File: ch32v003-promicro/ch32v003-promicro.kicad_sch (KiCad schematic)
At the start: 20 parts, among them J1 USB2.0_C_v3, J2 ProMicro-LeftPin, J3 ProMicro-RightPin, SW1 SW_Push, U1 CH32V003F4P6, U2 AMS1117-3.3, Y1 24M

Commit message: ch32v003promicro/1.0.0
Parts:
- added JP1: SolderJumper_2_Open, Jumper:SolderJumper-2_P1.3mm_Open_RoundedPad1.0x1.5mm, symbol Jumper:SolderJumper_2_Open
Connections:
- net +5V: now also JP1.1 (A)
- net +3V3 renamed VCC
- net VCC: now also JP1.2 (B)

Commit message: ch32v003promicro/1.1.0
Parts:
- removed C4, C5: 22p, $74th:Capacitor_0805_2012, symbol Device:C
- removed Y1: 24M, $74th:Crystal_SMD_3225-4Pin_3.2x2.5mm_HandSoldering, symbol Device:Crystal_GND24
- added C6: 1u, $74th:Capacitor_0805_2012, symbol Device:C
- added J2: SWD-MCU_Side-10Pin, $74th:SWD_2x05_P1.27mm, symbol $74th:SWD-MCU_Side-10Pin
- added R1: 10k, $74th:Register_0805_2012, symbol Device:R
- added R2: 54k, $74th:Register_0805_2012, symbol Device:R
- added R5: 1.5k(NC), $74th:Register_0805_2012, symbol Device:R
- added R6, R7: 27.4(NC), $74th:Register_0805_2012, symbol Device:R
- added U3: CH217K, Package_TO_SOT_SMD:SOT-23-6, symbol $74th:CH217K-USB_Power_Limit_Switch
- C2: renamed from C7; value 2.2u -> 10u
- D1: value LED -> Blue
- R10: renamed from R4; value 200 -> 10k
- renumbered C6 to C1, C1 to C3, C2 to C4, C3 to C5, J2 to J3, J3 to J4, R2 to R4, R5 to R8, R1 to R9, U2 to U1, U1 to U2
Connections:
- net +5V: now also U3.1 (VOUT); no longer J1.1 (VBUS)
- net 0/UART_RX: now also J2.7 (RXD)
- net 10/A10: now also U2.14 (PC4/ADC2); no longer U2.19 (PD2/ADC3)
- net 18/A0: now also U2.19 (PD2/ADC3); no longer U2.6 (PA2/ADC0/OSC_OUT)
- net 19/A1: now also U2.20 (PD3/UART_CTS/ADC4), R6.2; no longer U2.5 (PA1/ADC1/OSC_IN)
- net 1/UART_TX: now also J2.8 (TXD)
- net 21/A3: now also J2.2 (SWDIO)
- net 4/A6: now also U2.1 (PD4/UART_CK/ADC7), R7.2; no longer U2.20 (PD3/UART_CTS/ADC4)
- net 5: now also U2.5 (PA1/ADC1/OSC_IN); no longer U2.13 (PC3)
- net 6/A7: now also U2.6 (PA2/ADC0/OSC_OUT); no longer U2.1 (PD4/UART_CK/ADC7)
- net 7: now also U2.8 (PD0); no longer U2.10 (PC0)
- net 8/A8: now also U2.10 (PC0); no longer U2.8 (PD0)
- net 9/A9: now also U2.13 (PC3); no longer U2.14 (PC4/ADC2)
- net GND: now also C6.2, J2.3 (GND), J2.5 (GND), J2.9 (GND), R1.2, R2.2, U3.2 (GND)
- net RST: now also J2.10 (~{RESET})
- net VCC: now also C6.1, J2.1 (VCC), R5.1
- net USB_D-: now reaches J1.2 (D-)
- net USB_D-: now also R5.2, R6.1
- net USB_D+: now reaches J1.3 (D+)
- net USB_D+: now also R7.1
- net 16/SPI_MOSI renamed 16/SPL_MOSI
- new net: R1.1, U3.4 (EN#)
- new net: J1.1 (VBUS), U3.6 (VIN)
- new net: R2.1, U3.5 (ISET)
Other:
- note added: "CH32V003"
- note added: "ProMicro Pin"
- note added: "SWD 10pin with UART"
- note added: "USB"
- note added: "USB Data"
- note added: "VCC 5V Jumper"
- note added: "VCC Select"
- moved on the sheet: C1, C2, C3, C4, C5, D1, J1, JP1, R10, R3, R4, R8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

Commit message: ch32v003promicro/1.2.0
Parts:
- removed R1: 10k, $74th:Register_0805_2012, symbol Device:R
- removed R2: 54k, $74th:Register_0805_2012, symbol Device:R
- removed U3: CH217K, Package_TO_SOT_SMD:SOT-23-6, symbol $74th:CH217K-USB_Power_Limit_Switch
- added U3: CH213K, 74th:Package_SOT-23, symbol 74th_Passive:CH213K_Ideal-Diode-for-USB-Power
- C1, C2, C3, C4, C5, C6: footprint $74th:Capacitor_0805_2012 -> 74th:Capacitor_0805_2012
- D1: footprint $74th:LED_0805_2012Metric_Pad1.15x1.40mm_HandSolder -> 74th:LED_0805_2012
- J1: footprint $74th:USB-C-12-Pin-SMD -> 74th:Connector_USB-C-Receptacle_SMT_12-Pin_Simple
- J2: footprint $74th:SWD_2x05_P1.27mm -> 74th:Connector_HalfPinHeader_SWD
- J3: footprint $74th:ProMicro_LIKE_LEFT -> 74th:PinOut_ProMicro-LIKE_LEFT
- J4: footprint $74th:ProMicro_LIKE_RIGHT -> 74th:PinOut_ProMicro-LIKE_RIGHT
- R10, R3, R4, R5, R6, R7, R8, R9: footprint $74th:Register_0805_2012 -> 74th:Register_0805_2012
- SW1: footprint $74th:SKRPABE010 -> 74th:PushButton_SKRPABE010; Function (none) -> RST
- U1: footprint Package_TO_SOT_SMD:SOT-89-3 -> 74th:Package_SOT-89-3
- U2: footprint Package_SO:TSSOP-20_4.4x6.5mm_P0.65mm -> 74th:Package_TSSOP-20_4.4x6.5mm_P0.65mm
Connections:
- net +5V: now also U3.2 (VO-)
- net GND: now also U3.1 (GND)
- net at J1.1 (VBUS): now also U3.3 (VI+)
- no-connect marks 2 -> 1
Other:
- title: (none) -> CH32V003 ProMicro

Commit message: ch32v003promicto/1.3.0
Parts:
- removed C3, C5: 100n, 74th:Capacitor_0805_2012, symbol Device:C
- removed C6: 1u, 74th:Capacitor_0805_2012, symbol Device:C
- removed R5: 1.5k(NC), 74th:Register_0805_2012, symbol Device:R
- removed R6, R7: 27.4(NC), 74th:Register_0805_2012, symbol Device:R
- removed R8: 0, 74th:Register_0805_2012, symbol Device:R
- removed R9: 10k, 74th:Register_0805_2012, symbol Device:R
- added J5: SWD, 74th:PinOut_Pin_2_2GND, symbol 74th_Interface:SWD_WCH-1Wire
- C1, C2, C4: footprint 74th:Capacitor_0805_2012 -> 74th:Capacitor_0603_1608
- J1: symbol $74th:USB2.0_C_v3 -> 74th_Interface:USB_TypeC-2.0_Receptacle_Simple
- J2: symbol $74th:SWD-MCU_Side-10Pin -> 74th_Interface:SWD_10Pin_MCU-Side
- J3: symbol $74th:ProMicro-LeftPin -> 74th_Interface:ProMicro-Left
- J4: symbol $74th:ProMicro-RightPin -> 74th_Interface:ProMicro-Right
- JP1: footprint Jumper:SolderJumper-2_P1.3mm_Open_RoundedPad1.0x1.5mm -> 74th:SolderJumper-2
- R10, R3, R4: footprint 74th:Register_0805_2012 -> 74th:Register_0603_1608
- SW1: footprint 74th:PushButton_SKRPABE010 -> 74th:Switch_SKRPABE010
- U1: symbol Regulator_Linear:AMS1117-3.3 -> 74th_Passive:AMS1117-3.3_Regulator_SOT89
- U2: symbol $74th:CH32V003F4P6 -> 74th_MCU:CH32V003F4P6
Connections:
- net 2/I2C_SDA is gone; now on net PC1: J3.5 (2/SDA), U2.11 (PC1/I2C_SDA/SPI_NSS)
- net GND: now also J1.S1 (SHIELD), J5.2 (GND)
- net 0/UART_RX renamed PD6
- net 10/A10 renamed PC1
- net PC1: no longer U2.14 (PC4/ADC2)
- net 14/SPI_MISO renamed PC7
- net 15/SPI_SCK renamed PC5
- net 16/SPL_MOSI renamed PC6
- net 18/A0 renamed PD2
- net 19/A1 renamed PD3
- net 1/UART_TX renamed PD5
- net 20/A2 renamed PC4
- net PC4: now also U2.14 (PC4/ADC2)
- net 21/A3 renamed PD1
- net PD1: now also J5.1 (SWDIO)
- net 3/I2C_SCL renamed PC2
- net 4/A6 renamed PD4
- net 5 renamed PA1
- net 6/A7 renamed PA2
- net 7 renamed PD0
- net 8/A8 renamed PC0
- net 9/A9 renamed PC3
- net USB_D+: no longer names the net of J1.3 (D+)
- net USB_D-: no longer names the net of J1.2 (D-)
- no-connect marks 1 -> 3
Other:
- note removed: "USB Data"
- moved on the sheet: J2, J4, R3, R4, SW1

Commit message: fix silk
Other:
- note added: "CH32V00x"
- note removed: "CH32V003"
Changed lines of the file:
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@@
 	(title_block
 		(title "CH32V003 ProMicro")
-		(rev "v1.2.0")
+		(rev "v1.3.1")
 	)
 	(junction
@@
 		)
 	)
-	(text "CH32V003"
+	(text "CH32V00x"
 		(exclude_from_sim no)
 		(at 13.97 17.78 0)

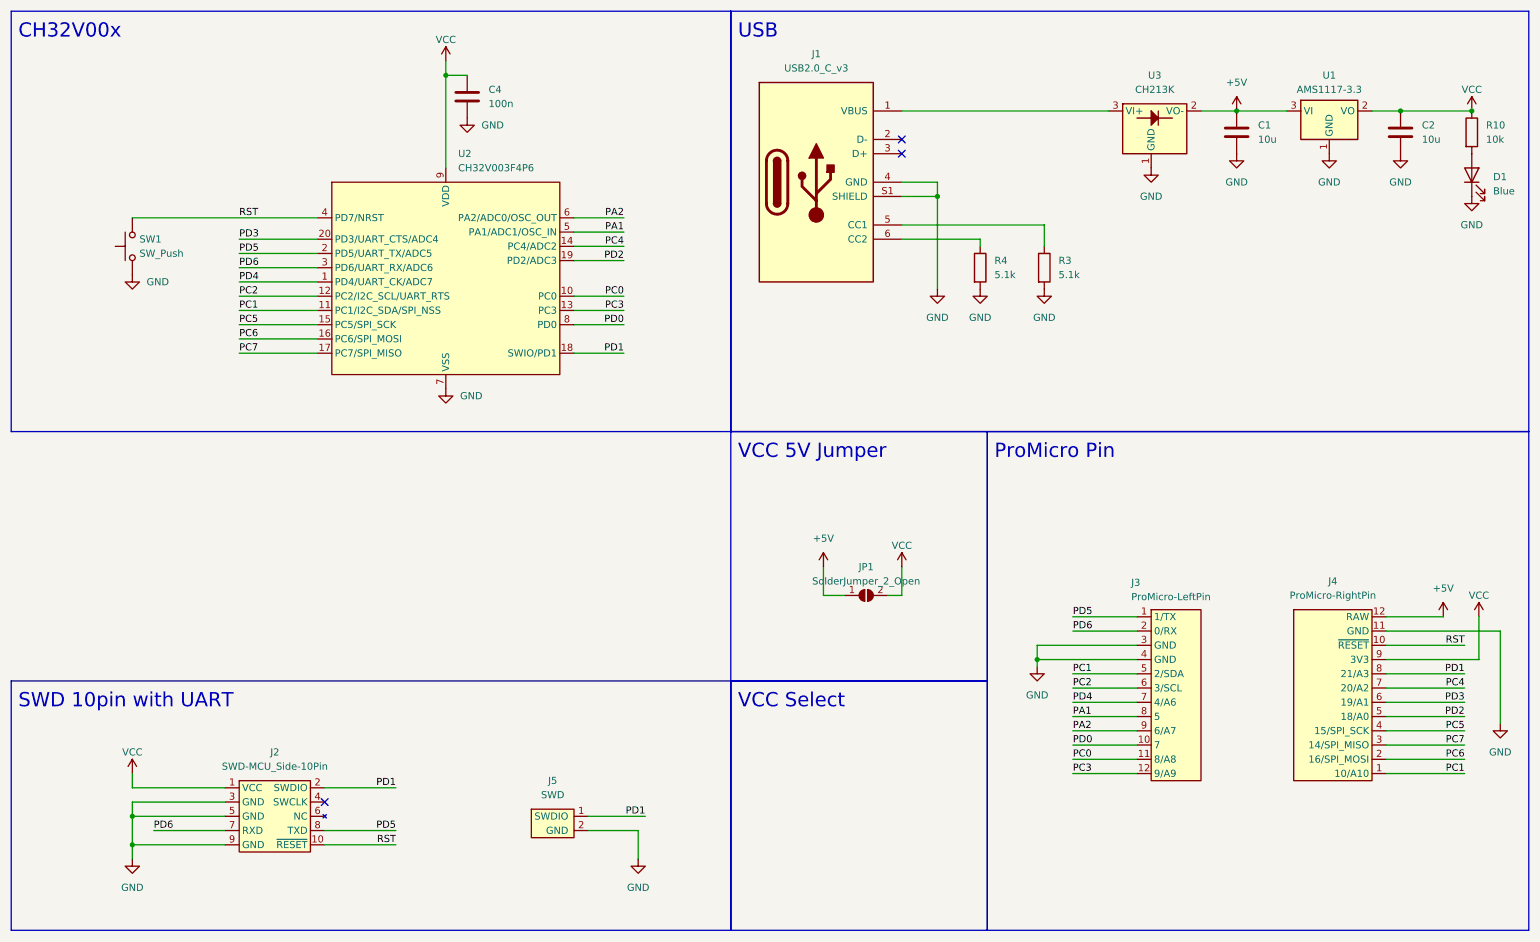
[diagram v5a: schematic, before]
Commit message: revert to ch32v003 v1.2.0
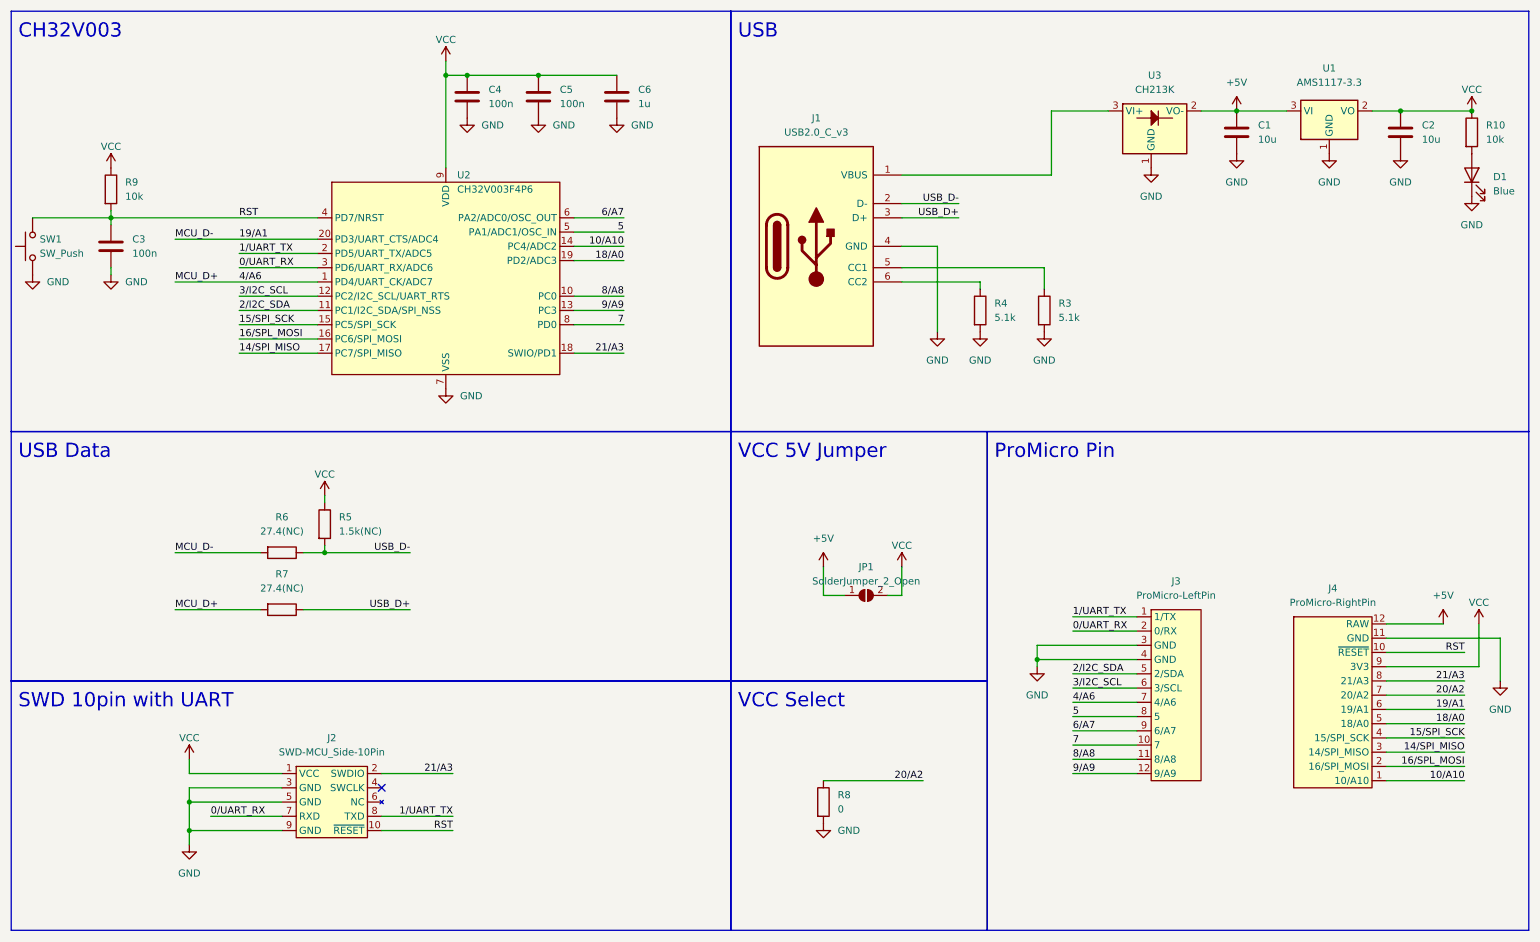
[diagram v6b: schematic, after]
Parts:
- removed J5: SWD, 74th:PinOut_Pin_2_2GND, symbol 74th_Interface:SWD_WCH-1Wire
- added C3, C5: 100n, 74th:Capacitor_0805_2012, symbol Device:C
- added C6: 1u, 74th:Capacitor_0805_2012, symbol Device:C
- added R5: 1.5k(NC), 74th:Register_0805_2012, symbol Device:R
- added R6, R7: 27.4(NC), 74th:Register_0805_2012, symbol Device:R
- added R8: 0, 74th:Register_0805_2012, symbol Device:R
- added R9: 10k, 74th:Register_0805_2012, symbol Device:R
- C1, C2, C4: footprint 74th:Capacitor_0603_1608 -> 74th:Capacitor_0805_2012
- J1: symbol 74th_Interface:USB_TypeC-2.0_Receptacle_Simple -> $74th:USB2.0_C_v3
- J2: symbol 74th_Interface:SWD_10Pin_MCU-Side -> $74th:SWD-MCU_Side-10Pin
- J3: symbol 74th_Interface:ProMicro-Left -> $74th:ProMicro-LeftPin
- J4: symbol 74th_Interface:ProMicro-Right -> $74th:ProMicro-RightPin
- JP1: footprint 74th:SolderJumper-2 -> Jumper:SolderJumper-2_P1.3mm_Open_RoundedPad1.0x1.5mm
- R10, R3, R4: footprint 74th:Register_0603_1608 -> 74th:Register_0805_2012
- SW1: footprint 74th:Switch_SKRPABE010 -> 74th:PushButton_SKRPABE010
- U1: symbol 74th_Passive:AMS1117-3.3_Regulator_SOT89 -> Regulator_Linear:AMS1117-3.3
- U2: symbol 74th_MCU:CH32V003F4P6 -> $74th:CH32V003F4P6
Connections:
- net GND: now also C3.2, C5.2, C6.2, R8.2; no longer J1.S1 (SHIELD)
- net RST: now also C3.1, R9.2
- net VCC: now also C5.1, C6.1, R5.1, R9.1
- net USB_D-: now reaches J1.2 (D-)
- net USB_D-: now also R5.2, R6.1
- net USB_D+: now reaches J1.3 (D+)
- net USB_D+: now also R7.1
- net PA1 renamed 5
- net PA2 renamed 6/A7
- net PC0 renamed 8/A8
- net PC1 renamed 2/I2C_SDA
- net 2/I2C_SDA: no longer J4.1 (10/A10)
- net PC2 renamed 3/I2C_SCL
- net PC3 renamed 9/A9
- net PC4 renamed 10/A10
- net 10/A10: now also J4.1 (10/A10); no longer J4.7 (20/A2)
- net PC5 renamed 15/SPI_SCK
- net PC6 renamed 16/SPL_MOSI
- net PC7 renamed 14/SPI_MISO
- net PD0 renamed 7
- net PD1 renamed 21/A3
- net PD2 renamed 18/A0
- net PD3 renamed 19/A1
- net 19/A1: now also R6.2
- net PD4 renamed 4/A6
- net 4/A6: now also R7.2
- net PD5 renamed 1/UART_TX
- net PD6 renamed 0/UART_RX
- new net 20/A2: J4.7 (20/A2), R8.1
- no-connect marks 3 -> 1
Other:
- note added: "CH32V003"
- note added: "USB Data"
- note removed: "CH32V00x"
- moved on the sheet: J2, J4, R3, R4, SW1
